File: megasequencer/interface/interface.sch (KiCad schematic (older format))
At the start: 55 parts, among them J1 INT_CLOCK_OUT, J10 OFFSET_A, J11 OFFSET_B, J12 OFFSET_C, J13 OFFSET_D, J14 OUTPUT_A, J15 OUTPUT_B, J16 OUTPUT_C, J17 OUTPUT_D, J18 OUTPUT_E, J19 OUTPUT_F, J2 EXT_CLOCK_IN, J20 TOP, J21 BOTTOM, J3 DIR_IN, J4 RESET_IN, J5 ZERO_IN, J6 STEP_OUT, J7 EXT_RATE_CV, J8 EXT_POS_CV, J9 PULSELEN_CV, SW1 CLOCK_SW, SW2 RESET_SW, SW3 ZERO_SW, SW4 SW_SPDT

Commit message: Finish interface and continue with brain
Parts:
- SW4: value SW_SPDT -> SEQ_DIR
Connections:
- net +5V: now also J21.15 (Pin_15), RV1.1, RV2.1, RV3.1; no longer RV1.3, RV2.3, RV3.3
- net EXT_POS_A: now also J21.9 (Pin_9)
- net EXT_RATE_A: now also J21.11 (Pin_11)
- net GND: now also H1.1, H2.1, H3.1, H4.1, J20.1 (Pin_1), J21.1 (Pin_1), J21.16 (Pin_16), RV1.3, RV2.3, RV3.3, RV4.3, RV5.3, RV6.3; no longer RV1.1, RV2.1, RV3.1, RV4.1, RV5.1, RV6.1
- net PULSELEN_A: now also J21.10 (Pin_10)
- net SEQ_DIR_D: now also J21.14 (Pin_14)
- net SEQ_RESET_D: now also J21.12 (Pin_12)
- net SEQ_ZERO_D: now also J21.13 (Pin_13)
- net at J7.T: now also RV4.1; no longer RV4.3
- net at J8.T: now also RV5.1; no longer RV5.3
- net at J9.T: now also RV6.1; no longer RV6.3
- no-connect marks 8 -> 16
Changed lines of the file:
@@
 AR Path="/5DDA0F22/5E04C279" Ref="SW?"  Part="1"
 F 0 "SW4" H 1700 2685 50  0000 C CNN
-F 1 "SW_SPDT" H 1700 2594 50  0000 C CNN
+F 1 "SEQ_DIR" H 1700 2594 50  0000 C CNN
 F 2 "Connector_PinSocket_2.54mm:PinSocket_1x03_P2.54mm_Vertical" H 1700 2400 50  0001 C CNN
 F 3 "" H 1700 2400 50  0001 C CNN
@@
 F 3 "~" H 4450 1650 50  0001 C CNN
 	1    4450 1650
-	-1   0    0    1
+	-1   0    0    -1
 $EndComp
 Wire Wire Line
@@
 F 3 "~" H 4000 950 50  0001 C CNN
 	1    4000 950
-	-1   0    0    1
+	-1   0    0    -1
 $EndComp
 $Comp
@@
 F 3 "~" H 4450 2950 50  0001 C CNN
 	1    4450 2950
-	-1   0    0    1
+	-1   0    0    -1
 $EndComp
 $Comp
@@
 F 3 "~" H 4000 2300 50  0001 C CNN
 	1    4000 2300
-	-1   0    0    1
+	-1   0    0    -1
 $EndComp
 Wire Wire Line
@@
 F 3 "~" H 4450 4350 50  0001 C CNN
 	1    4450 4350
-	-1   0    0    1
+	-1   0    0    -1
 $EndComp
 Wire Wire Line
@@
 F 3 "~" H 4000 3650 50  0001 C CNN
 	1    4000 3650
-	-1   0    0    1
+	-1   0    0    -1
 $EndComp
 $Comp
@@
 Wire Wire Line
 	8850 800  9050 800
-$Comp
-L power:+5V #PWR038
-U 1 1 5E2D31EE
-P 10650 850
-AR Path="/5E2D31EE" Ref="#PWR038"  Part="1"
-AR Path="/5DDA0F22/5E2D31EE" Ref="#PWR?"  Part="1"
-F 0 "#PWR038" H 10650 700 50  0001 C CNN
-F 1 "+5V" V 10650 1050 50  0000 C CNN
-F 2 "" H 10650 850 50  0001 C CNN
-F 3 "" H 10650 850 50  0001 C CNN
-	1    10650 850
-	0    1    1    0
-$EndComp
-Wire Wire Line
-	9600 900  9800 900
 Text Label 8850 1100 0    50   ~ 0
 OFFSET_B
@@
 Text Label 8850 1800 0    50   ~ 0
 OUTPUT_F
-Text Label 10650 2150 0    50   ~ 0
+Text Label 8850 3450 0    50   ~ 0
 EXT_RATE_A
-Text Label 10650 2250 0    50   ~ 0
+Text Label 8850 3650 0    50   ~ 0
 EXT_POS_A
-Text Label 10650 2350 0    50   ~ 0
+Text Label 8850 3550 0    50   ~ 0
 PULSELEN_A
 Text Label 8850 2000 0    50   ~ 0
@@
 Text Label 8850 1900 0    50   ~ 0
 EXT_CLOCK_D
-Text Label 9600 1100 0    50   ~ 0
+Text Label 8850 3150 0    50   ~ 0
 SEQ_DIR_D
-Text Label 9600 1300 0    50   ~ 0
+Text Label 8850 3350 0    50   ~ 0
 SEQ_RESET_D
-Text Label 9600 1200 0    50   ~ 0
+Text Label 8850 3250 0    50   ~ 0
 SEQ_ZERO_D
 Text Label 8850 2100 0    50   ~ 0
@@
 L power:+5V #PWR040
 U 1 1 5E2E5A57
-P 9850 3000
+P 9100 3050
 AR Path="/5E2E5A57" Ref="#PWR040"  Part="1"
 AR Path="/5DDA0F22/5E2E5A57" Ref="#PWR?"  Part="1"
-F 0 "#PWR040" H 9850 2850 50  0001 C CNN
-F 1 "+5V" V 9850 3200 50  0000 C CNN
-F 2 "" H 9850 3000 50  0001 C CNN
-F 3 "" H 9850 3000 50  0001 C CNN
-	1    9850 3000
-	0    1    1    0
-$EndComp
-Wire Wire Line
-	9600 3000 9850 3000
-$Comp
-L power:GND #PWR041
-U 1 1 5E2EB7CA
-P 9850 3100
-AR Path="/5E2EB7CA" Ref="#PWR041"  Part="1"
-AR Path="/5E36D63E/5E2EB7CA" Ref="#PWR?"  Part="1"
-F 0 "#PWR041" H 9850 2850 50  0001 C CNN
-F 1 "GND" V 9855 2972 50  0000 R CNN
-F 2 "" H 9850 3100 50  0001 C CNN
-F 3 "" H 9850 3100 50  0001 C CNN
-	1    9850 3100
-	0    -1   -1   0
-$EndComp
-Wire Wire Line
-	9600 3100 9850 3100
+F 0 "#PWR040" H 9100 2900 50  0001 C CNN
+F 1 "+5V" V 9100 3250 50  0000 C CNN
+F 2 "" H 9100 3050 50  0001 C CNN
+F 3 "" H 9100 3050 50  0001 C CNN
+	1    9100 3050
+	0    1    1    0
+$EndComp
+Wire Wire Line
+	8850 3050 9100 3050
 Text Notes 7050 6850 0    50   ~ 0
 This is the top layer of the Mega Sequencer. It contains all of the buttons, connectors and pots that are\nnot in the in the step matrix or part of the keyboard. It connects to the lower processing layer via a \n24 pin connector pointing downwards.
@@
 	-1   0    0    1
 $EndComp
+$Comp
+L power:GND #PWR0101
+U 1 1 5E0F7E36
+P 9100 2950
+AR Path="/5E0F7E36" Ref="#PWR0101"  Part="1"
+AR Path="/5E36D63E/5E0F7E36" Ref="#PWR?"  Part="1"
+F 0 "#PWR0101" H 9100 2700 50  0001 C CNN
+F 1 "GND" V 9105 2822 50  0000 R CNN
+F 2 "" H 9100 2950 50  0001 C CNN
+F 3 "" H 9100 2950 50  0001 C CNN
+	1    9100 2950
+	0    -1   -1   0
+$EndComp
+Wire Wire Line
+	8850 2950 9100 2950
+$Comp
+L power:GND #PWR0102
+U 1 1 5E197063
+P 9100 4450
+AR Path="/5E197063" Ref="#PWR0102"  Part="1"
+AR Path="/5E36D63E/5E197063" Ref="#PWR?"  Part="1"
+F 0 "#PWR0102" H 9100 4200 50  0001 C CNN
+F 1 "GND" V 9105 4322 50  0000 R CNN
+F 2 "" H 9100 4450 50  0001 C CNN
+F 3 "" H 9100 4450 50  0001 C CNN
+	1    9100 4450
+	0    -1   -1   0
+$EndComp
+$Comp
+L power:GND #PWR0103
+U 1 1 5E197874
+P 9100 2300
+AR Path="/5E197874" Ref="#PWR0103"  Part="1"
+AR Path="/5E36D63E/5E197874" Ref="#PWR?"  Part="1"
+F 0 "#PWR0103" H 9100 2050 50  0001 C CNN
+F 1 "GND" V 9105 2172 50  0000 R CNN
+F 2 "" H 9100 2300 50  0001 C CNN
+F 3 "" H 9100 2300 50  0001 C CNN
+	1    9100 2300
+	0    -1   -1   0
+$EndComp
+Wire Wire Line
+	8850 2300 9100 2300
+Wire Wire Line
+	8850 4450 9100 4450
+NoConn ~ 8850 2200
+NoConn ~ 8850 3750
+NoConn ~ 8850 3850
+NoConn ~ 8850 3950
+NoConn ~ 8850 4050
+NoConn ~ 8850 4150
+NoConn ~ 8850 4250
+NoConn ~ 8850 4350
+$Comp
+L power:GND #PWR?
+U 1 1 5E1D0467
+P 1900 7250
+AR Path="/5E1D0467" Ref="#PWR?"  Part="1"
+AR Path="/5DDA0F22/5E1D0467" Ref="#PWR?"  Part="1"
+F 0 "#PWR?" H 1900 7000 50  0001 C CNN
+F 1 "GND" H 1905 7077 50  0000 C CNN
+F 2 "" H 1900 7250 50  0001 C CNN
+F 3 "" H 1900 7250 50  0001 C CNN
+	1    1900 7250
+	1    0    0    -1
+$EndComp
+Wire Wire Line
+	850  7000 850  7150
+Wire Wire Line
+	850  7150 1200 7150
+Wire Wire Line
+	1900 7150 1900 7250
+Wire Wire Line
+	1900 7000 1900 7150
+Connection ~ 1900 7150
+Wire Wire Line
+	1550 7000 1550 7150
+Connection ~ 1550 7150
+Wire Wire Line
+	1550 7150 1900 7150
+Wire Wire Line
+	1200 7000 1200 7150
+Connection ~ 1200 7150
+Wire Wire Line
+	1200 7150 1550 7150
 $EndSCHEMATC

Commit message: Almost done now with both pcbs
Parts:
- added J22: RIGHT, Connector_PinHeader_2.54mm:PinHeader_1x04_P2.54mm_Vertical, symbol Connector_Generic:Conn_01x04
- J21: footprint Connector_PinHeader_2.54mm:PinHeader_1x16_P2.54mm_Vertical -> Connector_PinHeader_2.54mm:PinHeader_1x08_P2.54mm_Vertical; symbol Connector_Generic:Conn_01x16 -> Connector_Generic:Conn_01x08
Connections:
- net +5V: now also J21.7 (Pin_7); no longer J21.15 (Pin_15)
- net EXT_POS_A: now also J22.1 (Pin_1); no longer J21.9 (Pin_9)
- net EXT_RATE_A: now also J22.3 (Pin_3); no longer J21.11 (Pin_11)
- net GND: now also J21.8 (Pin_8), J22.4 (Pin_4); no longer J21.16 (Pin_16)
- net PULSELEN_A: now also J22.2 (Pin_2); no longer J21.10 (Pin_10)
- net SEQ_DIR_D: now also J21.6 (Pin_6); no longer J21.14 (Pin_14)
- net SEQ_RESET_D: now also J21.4 (Pin_4); no longer J21.12 (Pin_12)
- net SEQ_ZERO_D: now also J21.5 (Pin_5); no longer J21.13 (Pin_13)
- no-connect marks 16 -> 11
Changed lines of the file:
@@
 Text Label 8850 1800 0    50   ~ 0
 OUTPUT_F
-Text Label 8850 3450 0    50   ~ 0
+Text Label 8850 5050 0    50   ~ 0
 EXT_RATE_A
-Text Label 8850 3650 0    50   ~ 0
+Text Label 8850 5250 0    50   ~ 0
 EXT_POS_A
-Text Label 8850 3550 0    50   ~ 0
+Text Label 8850 5150 0    50   ~ 0
 PULSELEN_A
 Text Label 8850 2000 0    50   ~ 0
@@
 $EndComp
 $Comp
-L Connector_Generic:Conn_01x16 J21
+L Connector_Generic:Conn_01x08 J21
 U 1 1 5E4304E0
-P 8650 3750
-F 0 "J21" H 8568 2725 50  0000 C CNN
-F 1 "BOTTOM" H 8568 2816 50  0000 C CNN
-F 2 "Connector_PinHeader_2.54mm:PinHeader_1x16_P2.54mm_Vertical" H 8650 3750 50  0001 C CNN
-F 3 "~" H 8650 3750 50  0001 C CNN
-	1    8650 3750
+P 8650 3350
+F 0 "J21" H 8550 2700 50  0000 C CNN
+F 1 "BOTTOM" H 8550 2800 50  0000 C CNN
+F 2 "Connector_PinHeader_2.54mm:PinHeader_1x08_P2.54mm_Vertical" H 8650 3350 50  0001 C CNN
+F 3 "~" H 8650 3350 50  0001 C CNN
+	1    8650 3350
 	-1   0    0    1
 $EndComp
@@
 L power:GND #PWR0102
 U 1 1 5E197063
-P 9100 4450
+P 9100 3650
 AR Path="/5E197063" Ref="#PWR0102"  Part="1"
 AR Path="/5E36D63E/5E197063" Ref="#PWR?"  Part="1"
-F 0 "#PWR0102" H 9100 4200 50  0001 C CNN
-F 1 "GND" V 9105 4322 50  0000 R CNN
-F 2 "" H 9100 4450 50  0001 C CNN
-F 3 "" H 9100 4450 50  0001 C CNN
-	1    9100 4450
+F 0 "#PWR0102" H 9100 3400 50  0001 C CNN
+F 1 "GND" V 9105 3522 50  0000 R CNN
+F 2 "" H 9100 3650 50  0001 C CNN
+F 3 "" H 9100 3650 50  0001 C CNN
+	1    9100 3650
 	0    -1   -1   0
 $EndComp
@@
 	8850 2300 9100 2300
 Wire Wire Line
-	8850 4450 9100 4450
+	8850 3650 9100 3650
 NoConn ~ 8850 2200
-NoConn ~ 8850 3750
-NoConn ~ 8850 3850
-NoConn ~ 8850 3950
-NoConn ~ 8850 4050
-NoConn ~ 8850 4150
-NoConn ~ 8850 4250
-NoConn ~ 8850 4350
-$Comp
-L power:GND #PWR?
+NoConn ~ 8850 3450
+NoConn ~ 8850 3550
+$Comp
+L power:GND #PWR0104
 U 1 1 5E1D0467
 P 1900 7250
-AR Path="/5E1D0467" Ref="#PWR?"  Part="1"
+AR Path="/5E1D0467" Ref="#PWR0104"  Part="1"
 AR Path="/5DDA0F22/5E1D0467" Ref="#PWR?"  Part="1"
-F 0 "#PWR?" H 1900 7000 50  0001 C CNN
+F 0 "#PWR0104" H 1900 7000 50  0001 C CNN
 F 1 "GND" H 1905 7077 50  0000 C CNN
 F 2 "" H 1900 7250 50  0001 C CNN
@@
 Wire Wire Line
 	1200 7150 1550 7150
+$Comp
+L Connector_Generic:Conn_01x04 J22
+U 1 1 5E1FE22F
+P 8650 5150
+F 0 "J22" H 8568 4725 50  0000 C CNN
+F 1 "RIGHT" H 8568 4816 50  0000 C CNN
+F 2 "Connector_PinHeader_2.54mm:PinHeader_1x04_P2.54mm_Vertical" H 8650 5150 50  0001 C CNN
+F 3 "~" H 8650 5150 50  0001 C CNN
+	1    8650 5150
+	-1   0    0    1
+$EndComp
+$Comp
+L power:GND #PWR038
+U 1 1 5E233B4A
+P 9100 4950
+AR Path="/5E233B4A" Ref="#PWR038"  Part="1"
+AR Path="/5E36D63E/5E233B4A" Ref="#PWR?"  Part="1"
+F 0 "#PWR038" H 9100 4700 50  0001 C CNN
+F 1 "GND" V 9105 4822 50  0000 R CNN
+F 2 "" H 9100 4950 50  0001 C CNN
+F 3 "" H 9100 4950 50  0001 C CNN
+	1    9100 4950
+	0    -1   -1   0
+$EndComp
+Wire Wire Line
+	8850 4950 9100 4950
 $EndSCHEMATC

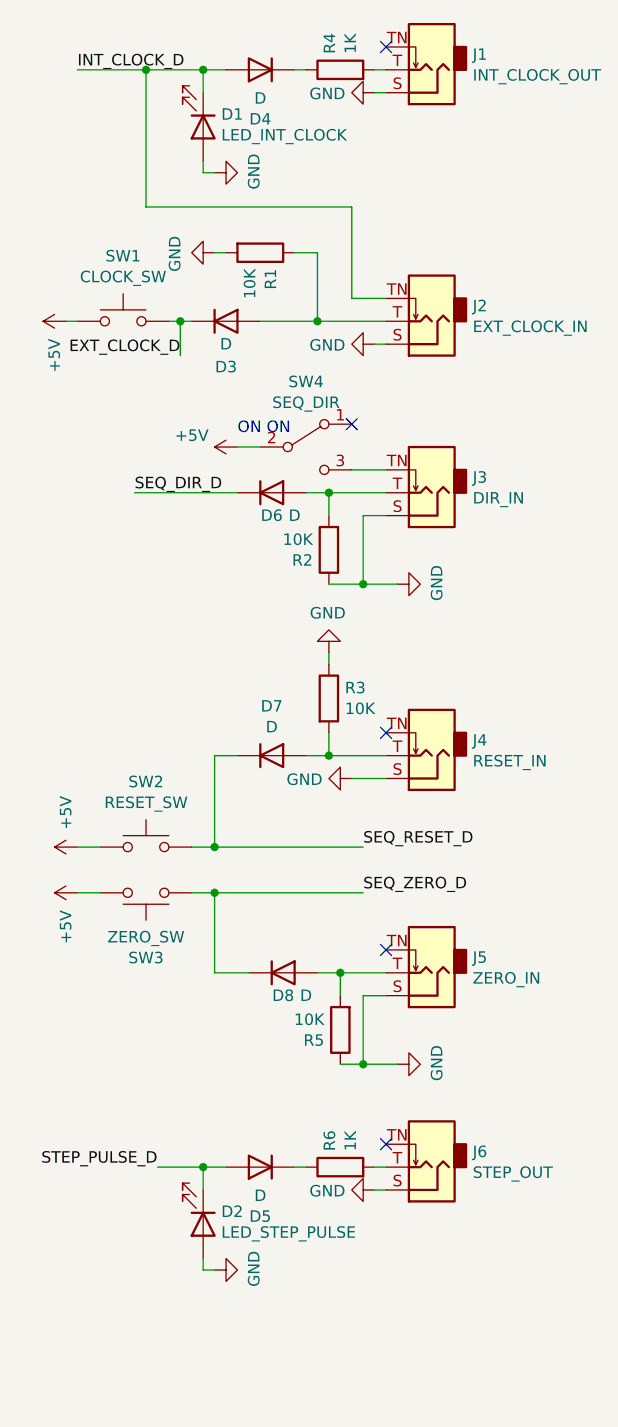
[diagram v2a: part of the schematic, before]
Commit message: Wrong LED direction
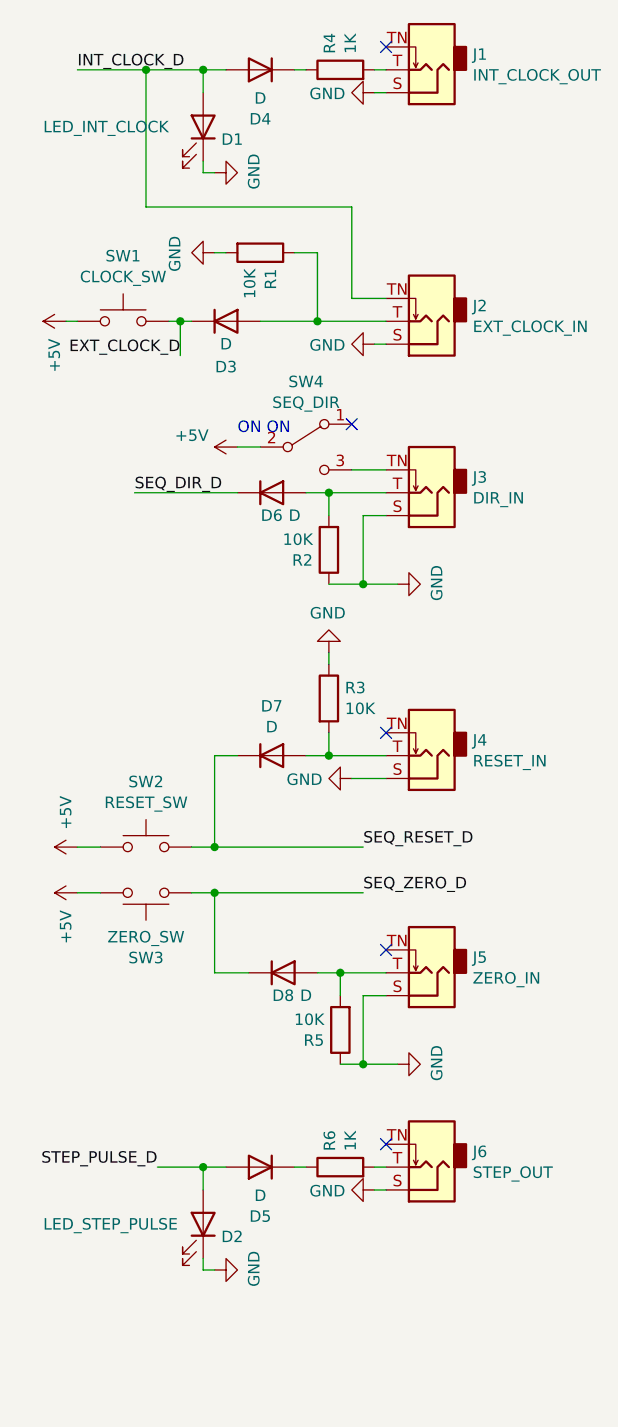
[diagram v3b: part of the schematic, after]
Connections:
- net GND: now also D1.1 (K), D2.1 (K); no longer D1.2 (A), D2.2 (A)
- net INT_CLOCK_D: now also D1.2 (A); no longer D1.1 (K)
- net STEP_PULSE_D: now also D2.2 (A); no longer D2.1 (K)
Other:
- moved on the sheet: D1, D2
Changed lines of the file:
@@
 EESchema Schematic File Version 4
-LIBS:interface-cache
 EELAYER 30 0
 EELAYER END
@@
 AR Path="/5DDA0F22/5E04C2A5" Ref="D?"  Part="1"
 F 0 "D1" V 1195 1079 50  0000 L CNN
-F 1 "LED_INT_CLOCK" V 1286 1079 50  0000 L CNN
+F 1 "LED_INT_CLOCK" V 1250 300 50  0000 L CNN
 F 2 "LED_THT:LED_D3.0mm" H 1250 1000 50  0001 C CNN
 F 3 "~" H 1250 1000 50  0001 C CNN
 	1    1250 1000
-	0    1    1    0
+	0    1    -1   0
 $EndComp
 $Comp
@@
 AR Path="/5DDA0F22/5E04C2DE" Ref="D?"  Part="1"
 F 0 "D2" V 1195 5879 50  0000 L CNN
-F 1 "LED_STEP_PULSE" V 1286 5879 50  0000 L CNN
+F 1 "LED_STEP_PULSE" V 1250 5100 50  0000 L CNN
 F 2 "LED_THT:LED_D3.0mm" H 1250 5800 50  0001 C CNN
 F 3 "~" H 1250 5800 50  0001 C CNN
 	1    1250 5800
-	0    1    1    0
-$EndComp
-$Comp
+	0    1    -1   0
+$EndComp
+$Comp
